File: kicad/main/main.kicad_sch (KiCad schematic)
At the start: 12 parts, among them M1 Stepper_Motor_bipolar, M2 Motor_Servo, SW1 SW_SPST, U1 S13V10FS, U2 L298, U3 BNO055, U4 BMP390, U5 BBB_Wireless

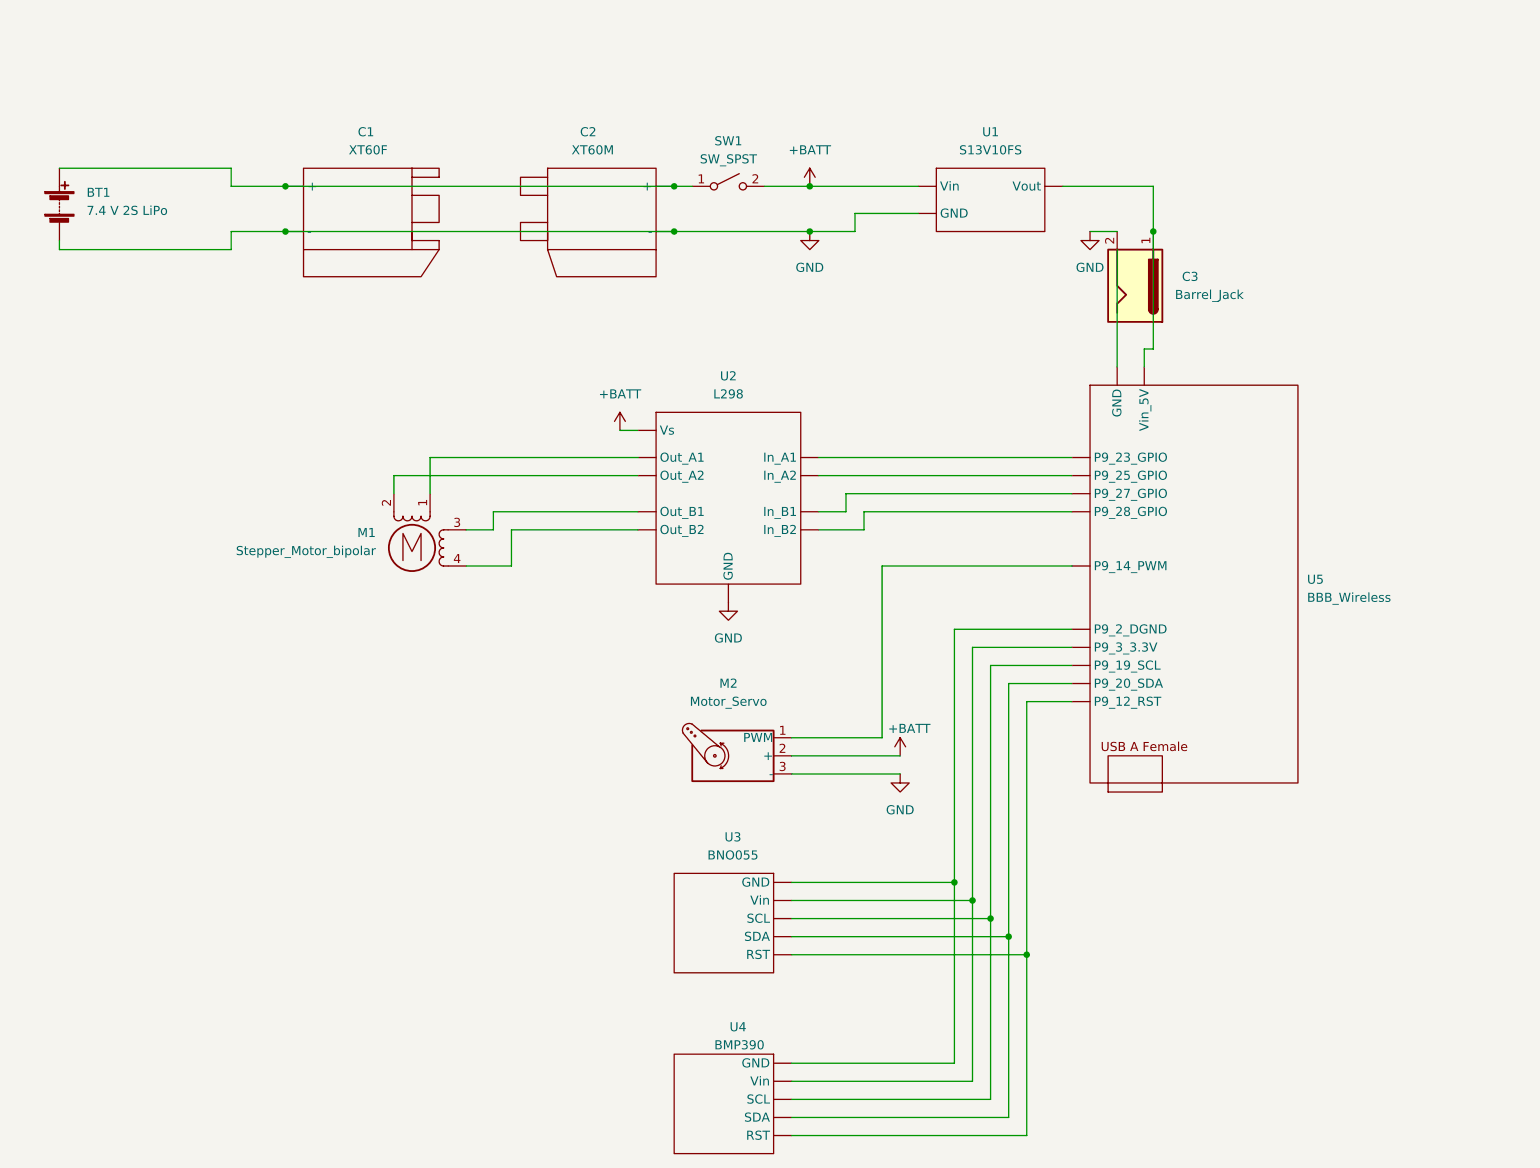
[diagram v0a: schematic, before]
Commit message: Changed library path, main_v1-4 and cam_v1-1 and Project-OWL block diagrams
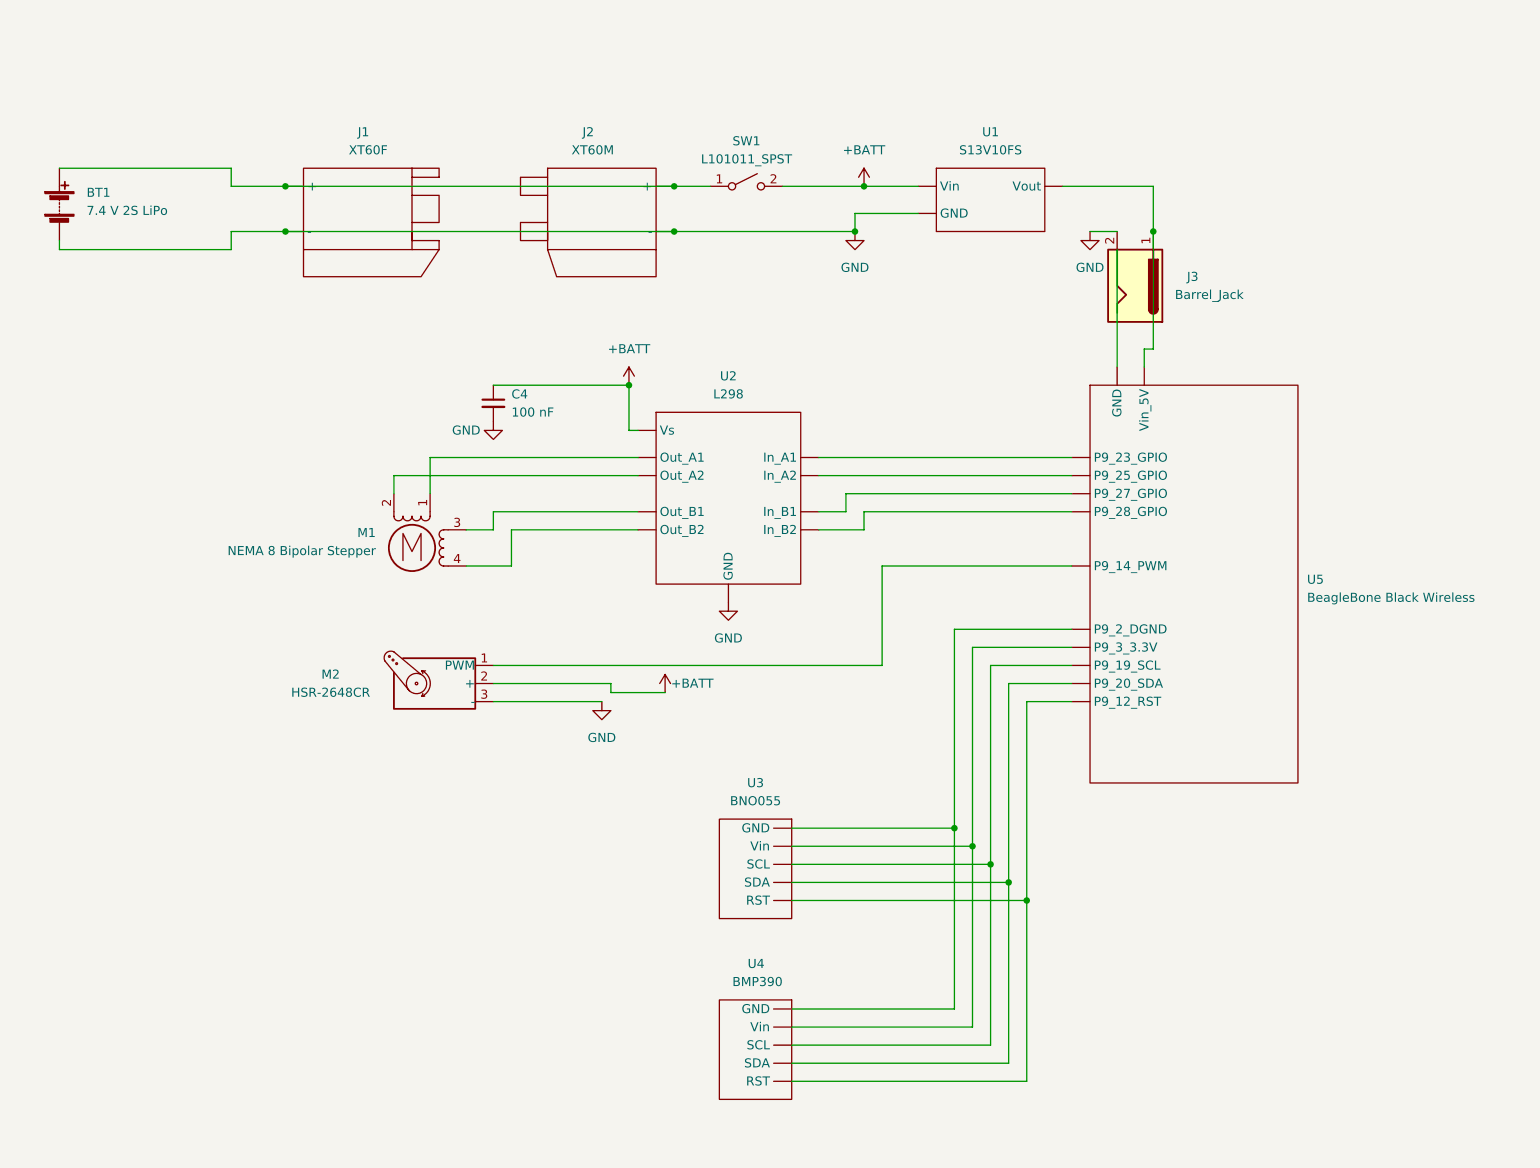
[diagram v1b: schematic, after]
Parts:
- added C4: 100 nF, symbol Device:C_Small
- M1: value Stepper_Motor_bipolar -> NEMA 8 Bipolar Stepper
- M2: value Motor_Servo -> HSR-2648CR
- SW1: value SW_SPST -> L101011_SPST
- U5: value BBB_Wireless -> BeagleBone Black Wireless
- renumbered C1 to J1, C2 to J2, C3 to J3
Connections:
- net +BATT: now also C4.1
- net GND: now also C4.2
- net at U5. (Vin_5V): now also U2. (Vs)
- new net: U3. (Vin), U4. (Vin), U5. (Vin_5V) (x4)
- new net: J3.1, U1. (Vout), U5. (Vin_5V)
- new net: U2. (Vs), U5. (Vin_5V) (x3)
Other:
- moved on the sheet: M2, SW1, U3, U4

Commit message: first working revision of cape done
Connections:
- net at U5. (Vin_5V): now also U2. (Vs)
- new net: U3. (Vin), U4. (Vin), U5. (Vin_5V) (x4)
- new net: J3.1, U1. (Vout), U5. (Vin_5V)
- new net: U2. (Vs), U5. (Vin_5V) (x3)

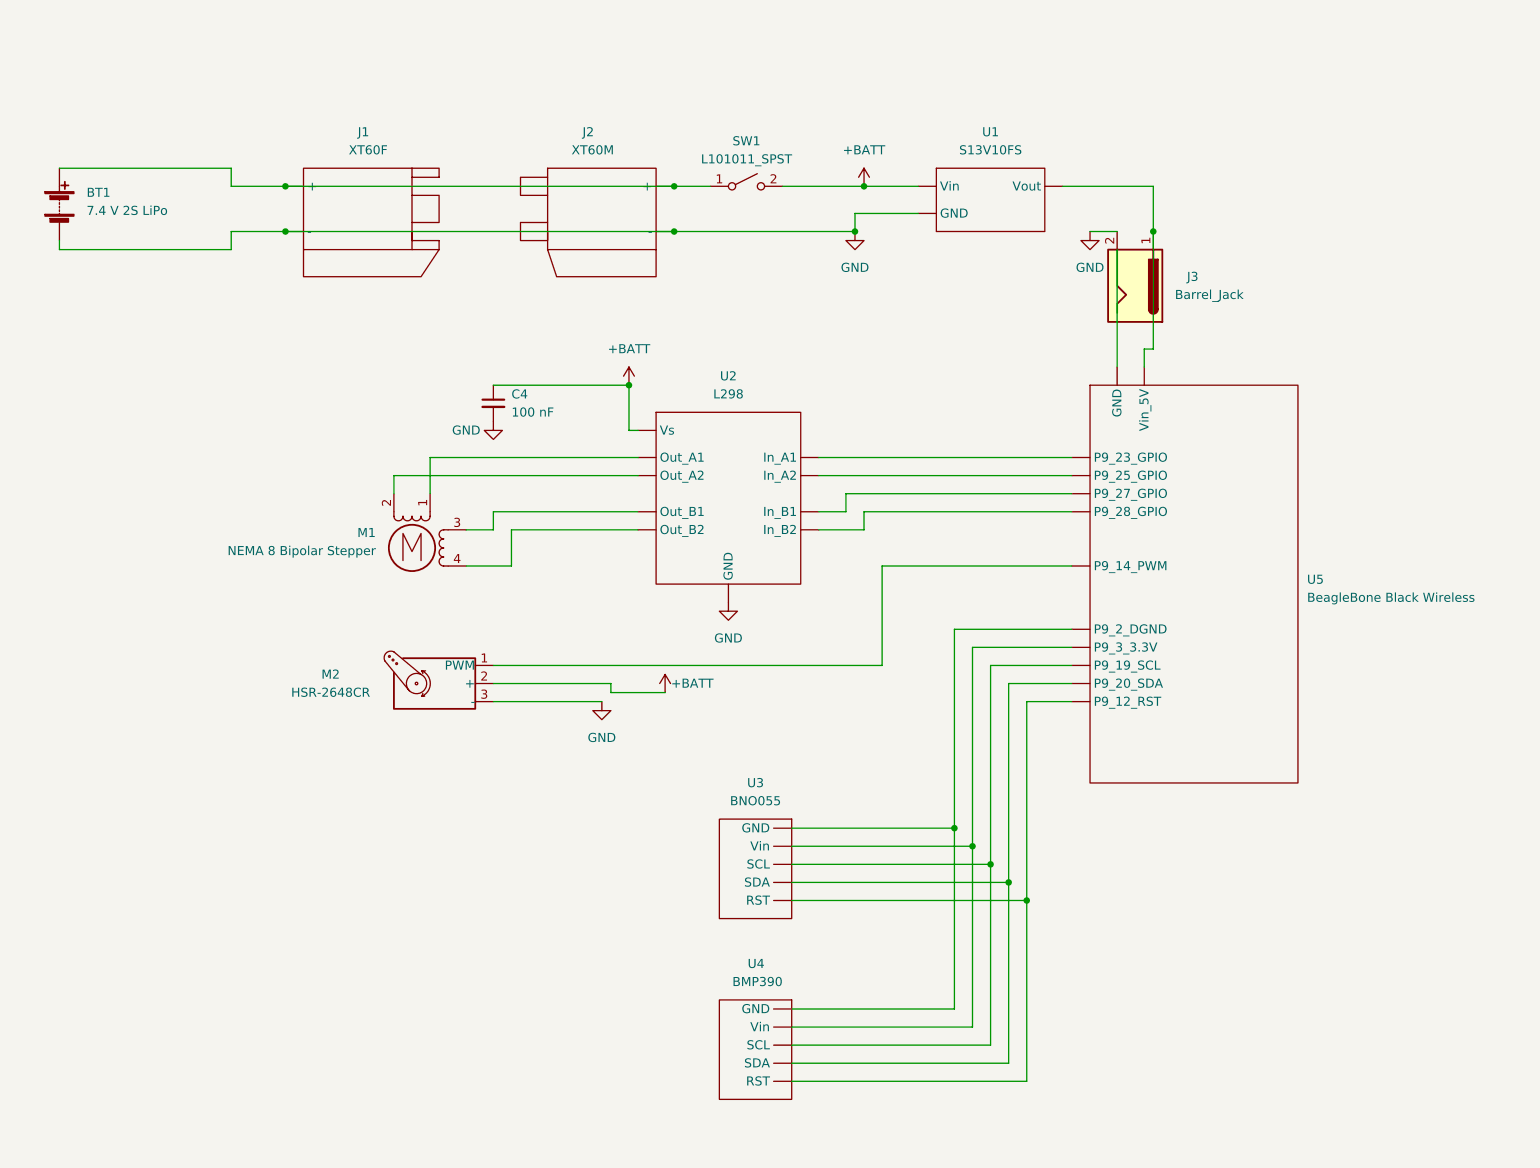
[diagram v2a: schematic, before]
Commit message: Updated main to 1.5
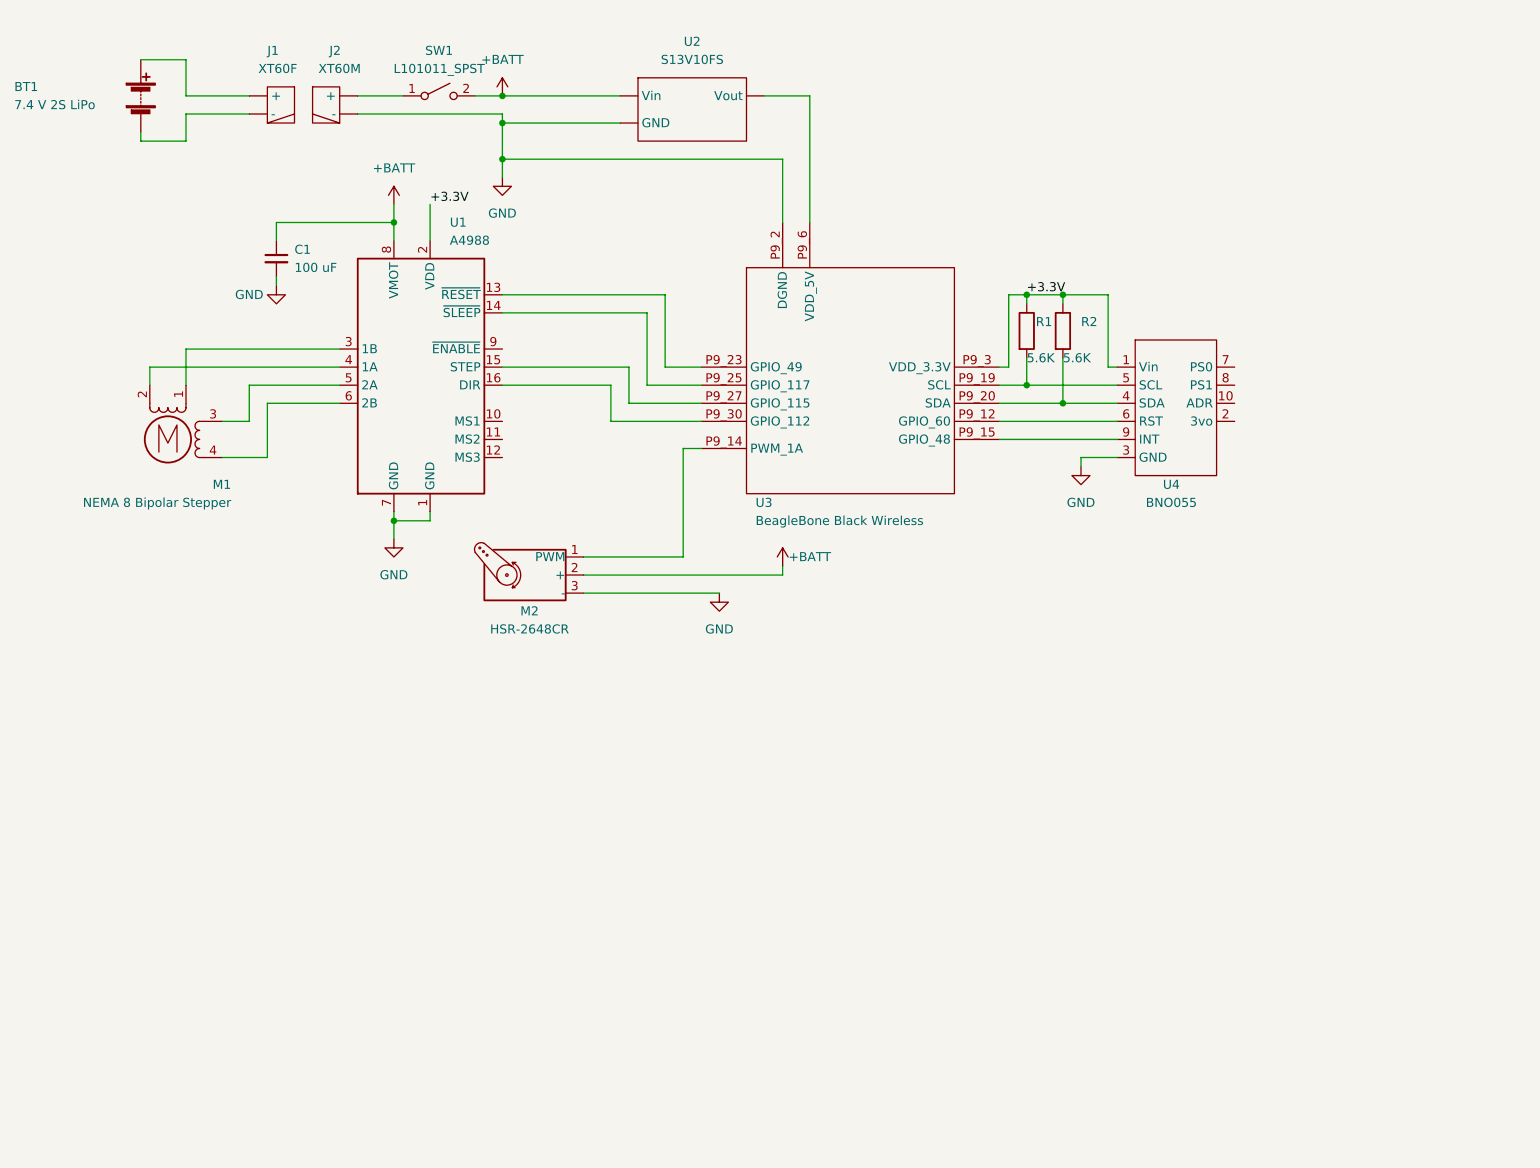
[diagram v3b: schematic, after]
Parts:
- removed J3: Barrel_Jack, symbol Connector:Barrel_Jack
- removed U2: L298, symbol payload_symbol_library:L298
- removed U4: BMP390, symbol payload_symbol_library:BMP390
- added R1, R2: 5.6K, symbol Device:R
- added U1: A4988, Module:Pololu_Breakout-16_15.2x20.3mm, symbol payload_symbol_library:A4988
- C1: renamed from C4; value 100 nF -> 100 uF
- renumbered U1 to U2, U5 to U3, U3 to U4
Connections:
- net +BATT: now also U1.8 (VMOT)
- net GND: now also U3.P9_2 (DGND), U4.3 (GND), U1.1 (GND), U1.7 (GND); no longer BT1.2 (-), J1. (-)
- net at M2.1 (PWM): now also U3.P9_14 (PWM_1A); no longer U3. (Vin_5V)
- net at M1.1: now also U1.3 (1B)
- net at M1.2 (-): now also U1.4 (1A)
- net at M1.3: now also U1.5 (2A)
- net at M1.4: now also U1.6 (2B)
- new net: U2. (Vout), U3.P9_6 (VDD_5V)
- new net: J2. (-), SW1.1 (A)
- new net: BT1.1 (+), J1. (-)
- new net: BT1.2 (-), J1. (-)
- new net: R2.2, U3.P9_20 (SDA), U4.4 (SDA)
- new net: U3.P9_12 (GPIO_60), U4.6 (RST)
- new net: U3.P9_15 (GPIO_48), U4.9 (INT)
- new net: R1.2, U3.P9_19 (SCL), U4.5 (SCL)
- new net: U1.13 (~{RESET}), U3.P9_23 (GPIO_49)
- new net: U1.14 (~{SLEEP}), U3.P9_25 (GPIO_117)
- new net: U1.15 (STEP), U3.P9_27 (GPIO_115)
- new net: U1.16 (DIR), U3.P9_30 (GPIO_112)
- new net +3.3V: R1.1, R2.1, U1.2 (VDD), U3.P9_3 (VDD_3.3V), U4.1 (Vin)
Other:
- title: Payload Main Circuit -> Payload Main System
- moved on the sheet: BT1, C1, M1, M2, SW1, U2

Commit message: Main 1.6, Cam 1.2, added pwr flags and not connected markers to eliminate ERC violations
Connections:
- net +BATT: now also U2.1 (Vin); no longer U2. (Vout)
- net GND: now also U2.2 (GND); no longer U2. (Vout)
- net at U3.P9_6 (VDD_5V): now also U2.3 (Vout); no longer U2. (Vout)
- no-connect marks 0 -> 8
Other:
- title: Payload Main System -> Payload Main Subsystem
- moved on the sheet: J1, J2, SW1

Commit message: Cape v 1.2
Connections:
- net at M2.1 (PWM): now also U3.P8_13 (PWM_2B); no longer U3.P9_14 (PWM_1A)
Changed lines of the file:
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@@
       (effects (font (size 1.27 1.27)) hide)
     )
+    (pin "P8_13")
     (pin "P9_12")
-    (pin "P9_14")
     (pin "P9_15")
     (pin "P9_19")
